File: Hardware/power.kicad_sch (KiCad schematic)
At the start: 13 parts, among them J2 USB_C_Receptacle, U3 ADP2164ACPZ-3.3-R7

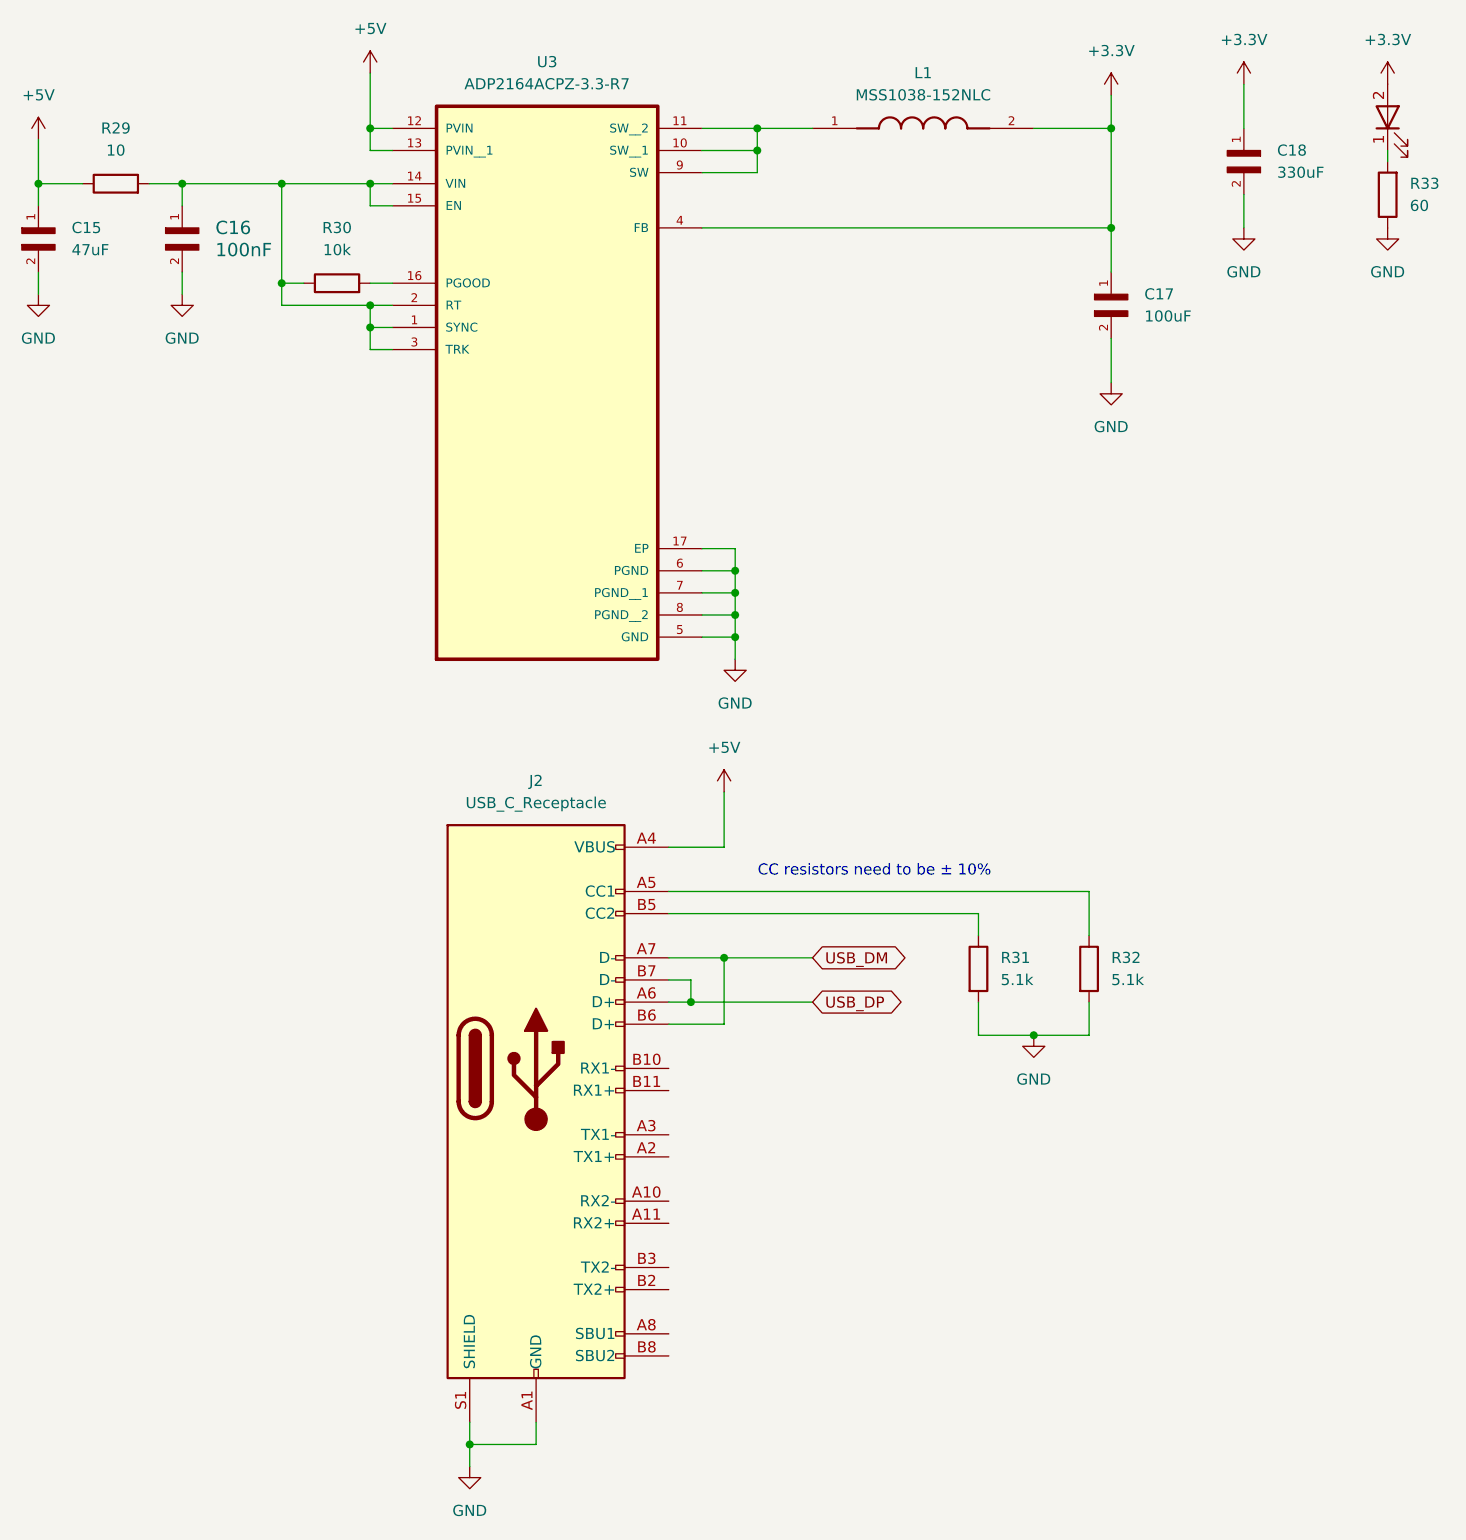
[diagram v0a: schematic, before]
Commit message: added stackup doc and reduced board to 10 layers
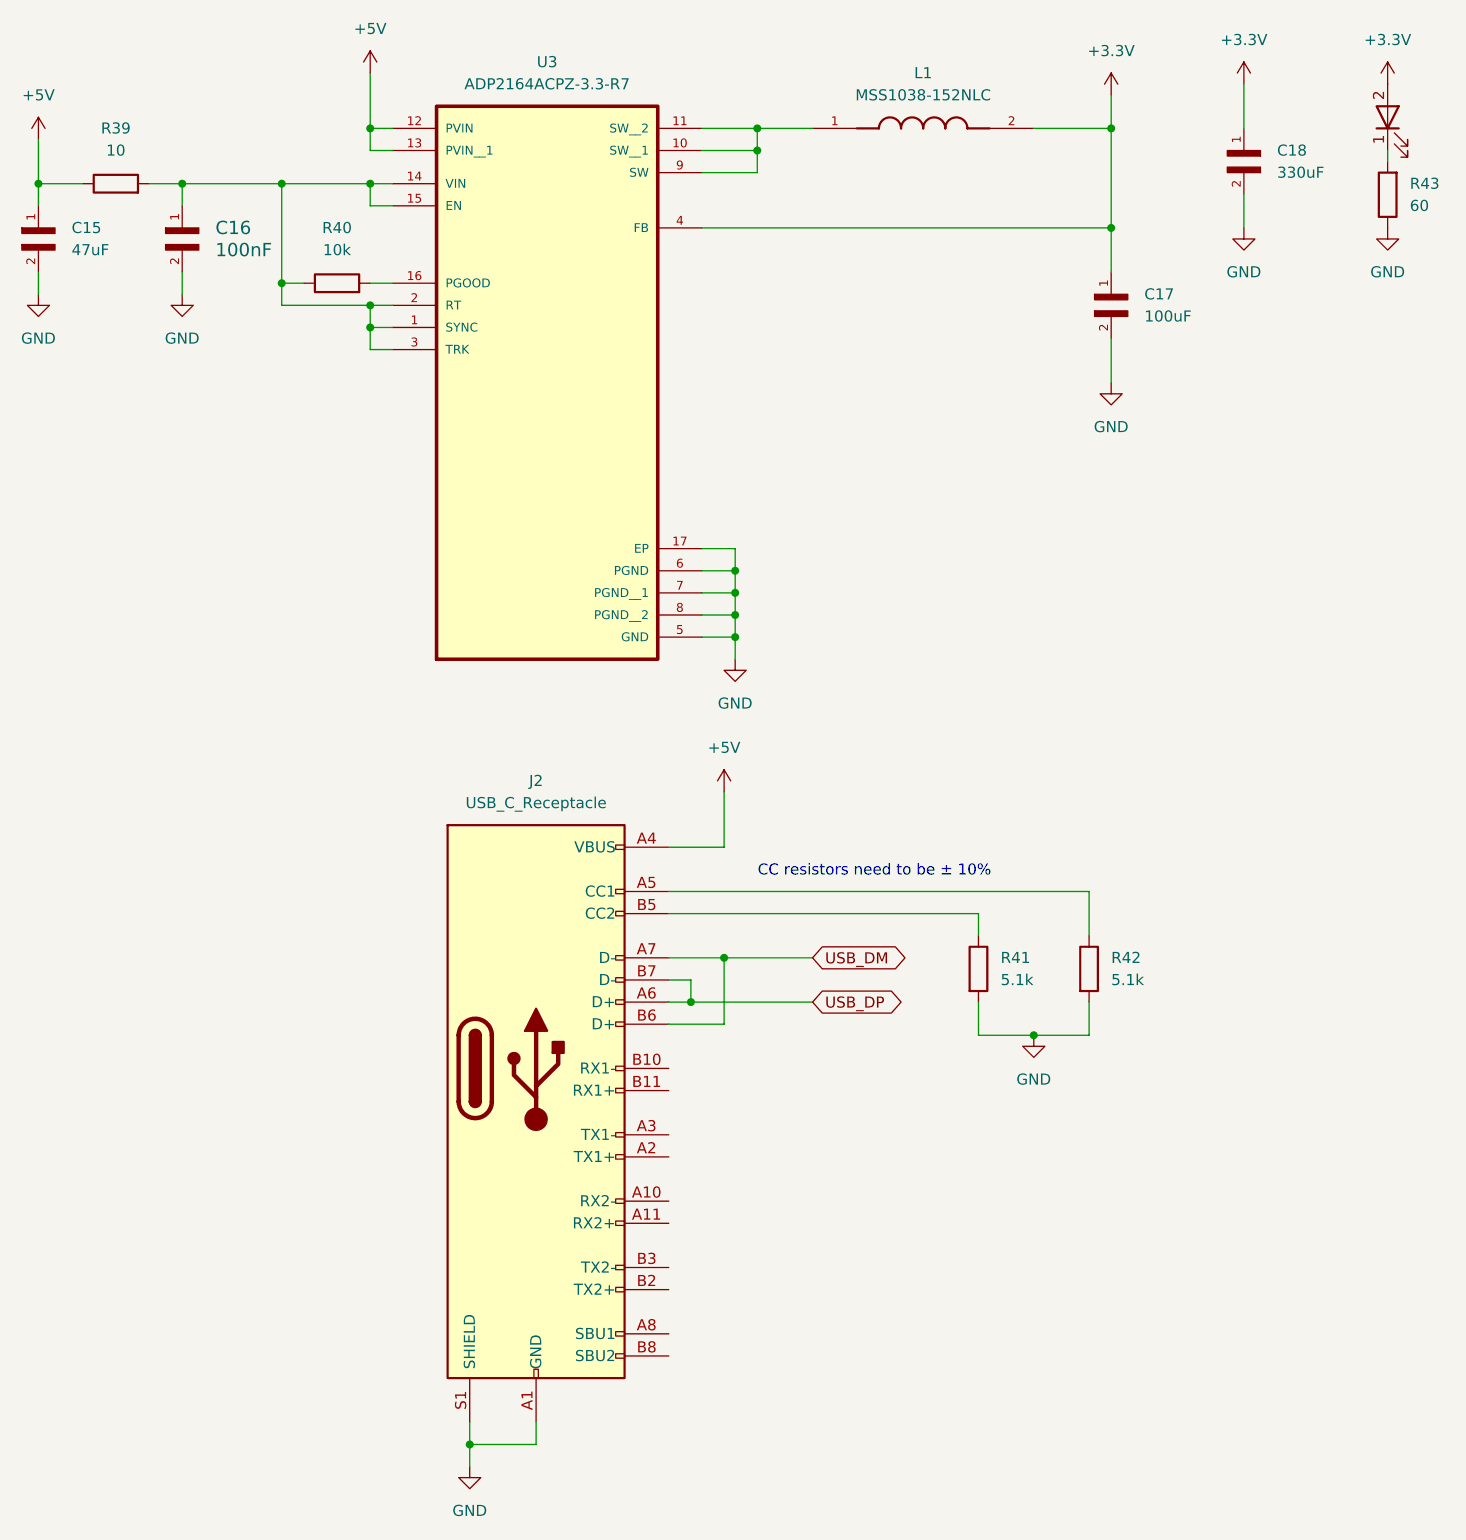
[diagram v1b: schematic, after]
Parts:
- renumbered LED1 to LED9, R29 to R39, R30 to R40, R31 to R41, R32 to R42, R33 to R43
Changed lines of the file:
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@@
 		(dnp no)
 		(fields_autoplaced yes)
-		(property "Reference" "R29"
+		(property "Reference" "R39"
 			(at 36.83 34.29 90)
 			(effects
@@
 			(project "Radio Project"
 				(path "/ca6389fe-9846-40e3-87a4-456cfcfc0777/bd0f5978-e4b1-41e2-96b4-94a3773ac12f"
-					(reference "R29")
+					(reference "R39")
 					(unit 1)
 				)
@@
 		(dnp no)
 		(fields_autoplaced yes)
-		(property "Reference" "#PWR023"
+		(property "Reference" "#PWR031"
 			(at 77.47 194.31 0)
 			(effects
@@
 			(project "Radio Project"
 				(path "/ca6389fe-9846-40e3-87a4-456cfcfc0777/bd0f5978-e4b1-41e2-96b4-94a3773ac12f"
-					(reference "#PWR023")
+					(reference "#PWR031")
 					(unit 1)
 				)
@@
 		(dnp no)
 		(fields_autoplaced yes)
-		(property "Reference" "#PWR027"
+		(property "Reference" "#PWR035"
 			(at 151.13 34.29 0)
 			(effects
@@
 			(project "Radio Project"
 				(path "/ca6389fe-9846-40e3-87a4-456cfcfc0777/bd0f5978-e4b1-41e2-96b4-94a3773ac12f"
-					(reference "#PWR027")
+					(reference "#PWR035")
 					(unit 1)
 				)
@@
 		(dnp no)
 		(fields_autoplaced yes)
-		(property "Reference" "#PWR024"
+		(property "Reference" "#PWR032"
 			(at 106.68 114.3 0)
 			(effects
@@
 			(project "Radio Project"
 				(path "/ca6389fe-9846-40e3-87a4-456cfcfc0777/bd0f5978-e4b1-41e2-96b4-94a3773ac12f"
-					(reference "#PWR024")
+					(reference "#PWR032")
 					(unit 1)
 				)
@@
 		(dnp no)
 		(fields_autoplaced yes)
-		(property "Reference" "#PWR019"
+		(property "Reference" "#PWR027"
 			(at 27.94 39.37 0)
 			(effects
@@
 			(project "Radio Project"
 				(path "/ca6389fe-9846-40e3-87a4-456cfcfc0777/bd0f5978-e4b1-41e2-96b4-94a3773ac12f"
-					(reference "#PWR019")
+					(reference "#PWR027")
 					(unit 1)
 				)
@@
 		(dnp no)
 		(fields_autoplaced yes)
-		(property "Reference" "R33"
+		(property "Reference" "R43"
 			(at 185.42 40.6399 0)
 			(effects
@@
 			(project "Radio Project"
 				(path "/ca6389fe-9846-40e3-87a4-456cfcfc0777/bd0f5978-e4b1-41e2-96b4-94a3773ac12f"
-					(reference "R33")
+					(reference "R43")
 					(unit 1)
 				)
@@
 		(dnp no)
 		(fields_autoplaced yes)
-		(property "Reference" "#PWR029"
+		(property "Reference" "#PWR037"
 			(at 166.37 33.02 0)
 			(effects
@@
 			(project "Radio Project"
 				(path "/ca6389fe-9846-40e3-87a4-456cfcfc0777/bd0f5978-e4b1-41e2-96b4-94a3773ac12f"
-					(reference "#PWR029")
+					(reference "#PWR037")
 					(unit 1)
 				)
@@
 		(dnp no)
 		(fields_autoplaced yes)
-		(property "Reference" "LED1"
+		(property "Reference" "LED9"
 			(at 172.72 15.24 0)
 			(effects
@@
 			(project ""
 				(path "/ca6389fe-9846-40e3-87a4-456cfcfc0777/bd0f5978-e4b1-41e2-96b4-94a3773ac12f"
-					(reference "LED1")
+					(reference "LED9")
 					(unit 1)
 				)
@@
 		(dnp no)
 		(fields_autoplaced yes)
-		(property "Reference" "#PWR025"
+		(property "Reference" "#PWR033"
 			(at 107.95 101.6 0)
 			(effects
@@
 			(project ""
 				(path "/ca6389fe-9846-40e3-87a4-456cfcfc0777/bd0f5978-e4b1-41e2-96b4-94a3773ac12f"
-					(reference "#PWR025")
+					(reference "#PWR033")
 					(unit 1)
 				)
@@
 		(dnp no)
 		(fields_autoplaced yes)
-		(property "Reference" "#PWR026"
+		(property "Reference" "#PWR034"
 			(at 142.24 144.78 0)
 			(effects
@@
 			(project "Radio Project"
 				(path "/ca6389fe-9846-40e3-87a4-456cfcfc0777/bd0f5978-e4b1-41e2-96b4-94a3773ac12f"
-					(reference "#PWR026")
+					(reference "#PWR034")
 					(unit 1)
 				)
@@
 		(dnp no)
 		(fields_autoplaced yes)
-		(property "Reference" "R31"
+		(property "Reference" "R41"
 			(at 138.43 129.5399 0)
 			(effects
@@
 			(project "Radio Project"
 				(path "/ca6389fe-9846-40e3-87a4-456cfcfc0777/bd0f5978-e4b1-41e2-96b4-94a3773ac12f"
-					(reference "R31")
+					(reference "R41")
 					(unit 1)
 				)
@@
 		(dnp no)
 		(fields_autoplaced yes)
-		(property "Reference" "#PWR031"
+		(property "Reference" "#PWR039"
 			(at 182.88 33.02 0)
 			(effects
@@
 			(project "Radio Project"
 				(path "/ca6389fe-9846-40e3-87a4-456cfcfc0777/bd0f5978-e4b1-41e2-96b4-94a3773ac12f"
-					(reference "#PWR031")
+					(reference "#PWR039")
 					(unit 1)
 				)
@@
 		(dnp no)
 		(fields_autoplaced yes)
-		(property "Reference" "#PWR028"
+		(property "Reference" "#PWR036"
 			(at 151.13 69.85 0)
 			(effects
@@
 			(project "Radio Project"
 				(path "/ca6389fe-9846-40e3-87a4-456cfcfc0777/bd0f5978-e4b1-41e2-96b4-94a3773ac12f"
-					(reference "#PWR028")
+					(reference "#PWR036")
 					(unit 1)
 				)
@@
 		(dnp no)
 		(fields_autoplaced yes)
-		(property "Reference" "#PWR021"
+		(property "Reference" "#PWR029"
 			(at 44.45 59.69 0)
 			(effects
@@
 			(project "Radio Project"
 				(path "/ca6389fe-9846-40e3-87a4-456cfcfc0777/bd0f5978-e4b1-41e2-96b4-94a3773ac12f"
-					(reference "#PWR021")
+					(reference "#PWR029")
 					(unit 1)
 				)
@@
 		(dnp no)
 		(fields_autoplaced yes)
-		(property "Reference" "#PWR032"
+		(property "Reference" "#PWR040"
 			(at 182.88 52.07 0)
 			(effects
@@
 			(project "Radio Project"
 				(path "/ca6389fe-9846-40e3-87a4-456cfcfc0777/bd0f5978-e4b1-41e2-96b4-94a3773ac12f"
-					(reference "#PWR032")
+					(reference "#PWR040")
 					(unit 1)
 				)
@@
 		(dnp no)
 		(fields_autoplaced yes)
-		(property "Reference" "#PWR022"
+		(property "Reference" "#PWR030"
 			(at 66.04 31.75 0)
 			(effects
@@
 			(project ""
 				(path "/ca6389fe-9846-40e3-87a4-456cfcfc0777/bd0f5978-e4b1-41e2-96b4-94a3773ac12f"
-					(reference "#PWR022")
+					(reference "#PWR030")
 					(unit 1)
 				)
@@
 		(dnp no)
 		(fields_autoplaced yes)
-		(property "Reference" "#PWR020"
+		(property "Reference" "#PWR028"
 			(at 27.94 59.69 0)
 			(effects
@@
 			(project "Radio Project"
 				(path "/ca6389fe-9846-40e3-87a4-456cfcfc0777/bd0f5978-e4b1-41e2-96b4-94a3773ac12f"
-					(reference "#PWR020")
+					(reference "#PWR028")
 					(unit 1)
 				)
@@
 		(dnp no)
 		(fields_autoplaced yes)
-		(property "Reference" "R30"
+		(property "Reference" "R40"
 			(at 62.23 45.72 90)
 			(effects
@@
 			(project "Radio Project"
 				(path "/ca6389fe-9846-40e3-87a4-456cfcfc0777/bd0f5978-e4b1-41e2-96b4-94a3773ac12f"
-					(reference "R30")
+					(reference "R40")
 					(unit 1)
 				)
@@
 		(dnp no)
 		(fields_autoplaced yes)
-		(property "Reference" "R32"
+		(property "Reference" "R42"
 			(at 151.13 129.5399 0)
 			(effects
@@
 			(project "Radio Project"
 				(path "/ca6389fe-9846-40e3-87a4-456cfcfc0777/bd0f5978-e4b1-41e2-96b4-94a3773ac12f"
-					(reference "R32")
+					(reference "R42")
 					(unit 1)
 				)
@@
 		(dnp no)
 		(fields_autoplaced yes)
-		(property "Reference" "#PWR030"
+		(property "Reference" "#PWR038"
 			(at 166.37 52.07 0)
 			(effects
@@
 			(project "Radio Project"
 				(path "/ca6389fe-9846-40e3-87a4-456cfcfc0777/bd0f5978-e4b1-41e2-96b4-94a3773ac12f"
-					(reference "#PWR030")
-					(unit 1)
-				)
+					(reference "#PWR038")
+					(unit 1)
+				)

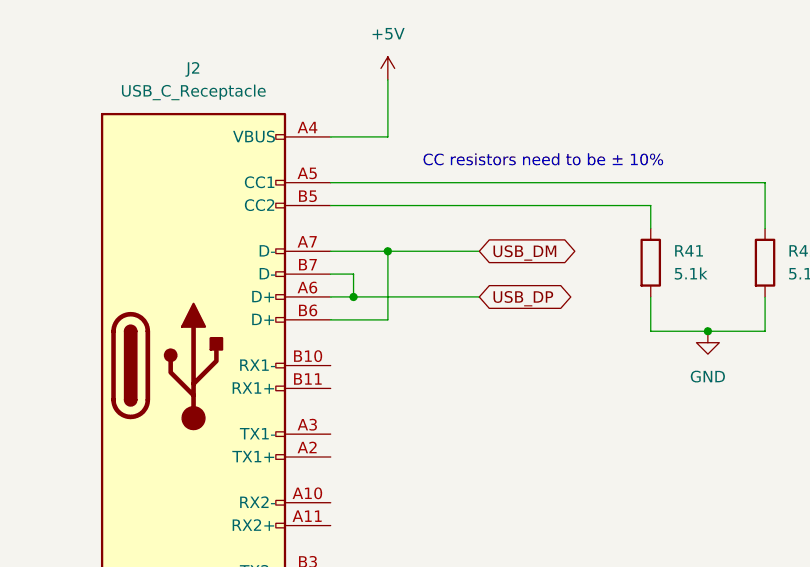
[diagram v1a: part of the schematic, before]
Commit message: fixed USB data lines and directory hierarchy
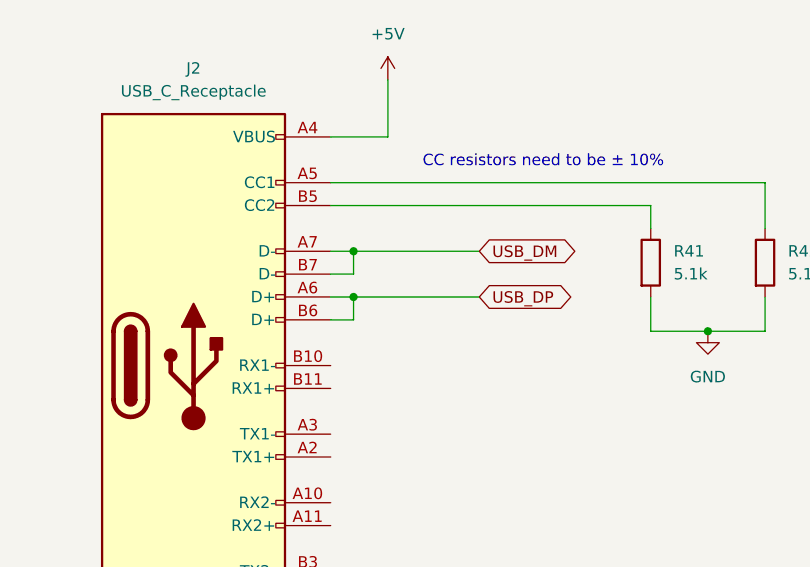
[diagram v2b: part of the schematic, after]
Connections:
- net USB_DM: now also J2.B7 (D-); no longer J2.B6 (D+)
- net USB_DP: now also J2.B6 (D+); no longer J2.B7 (D-)

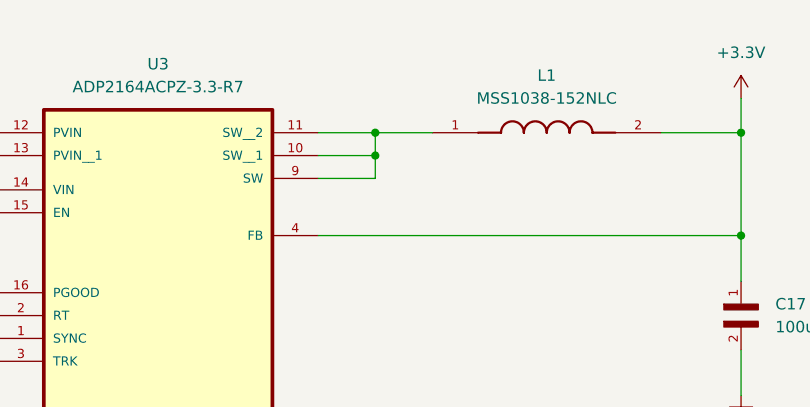
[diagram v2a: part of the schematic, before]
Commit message: diff pair routing for ethernet
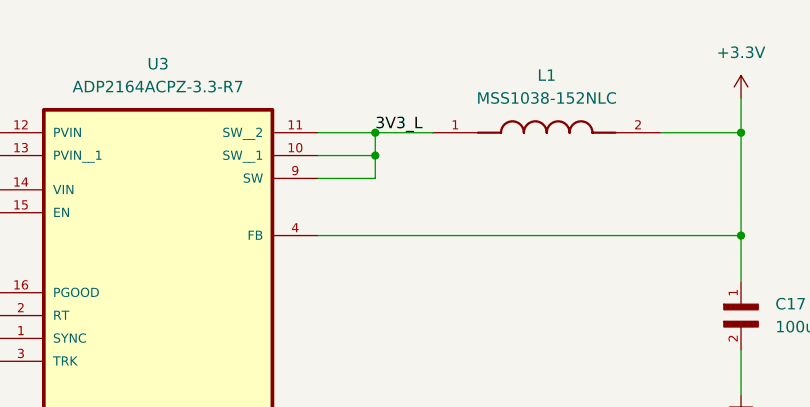
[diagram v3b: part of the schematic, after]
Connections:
- net 3V3_L: now reaches L1.1, U3.10 (SW__1), U3.11 (SW__2), U3.9 (SW)
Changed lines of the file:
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@@
+		)
+	)
+	(label "3V3_L"
+		(at 110.49 34.29 0)
+		(effects
+			(font
+				(size 1.27 1.27)
+			)
+			(justify left bottom)
 		)
 	)
